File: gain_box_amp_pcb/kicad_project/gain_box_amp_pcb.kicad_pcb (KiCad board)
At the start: 2 copper layers, 80 x 100 mm, 58 parts, among them J1 Conn_01x02, J2 Conn_01x02, J3 Conn_01x02, J4 Conn_01x02, J5 Conn_01x02, J6 Conn_01x02, J7 Conn_01x02, J8 Conn_01x03, J9 Conn_01x04, K1 J104D2C12VDC.36S, K2 J104D2C12VDC.36S, K3 G5V-1, U1 NE5532, U2 NE5532, U3 NE5532, U4 140817141310

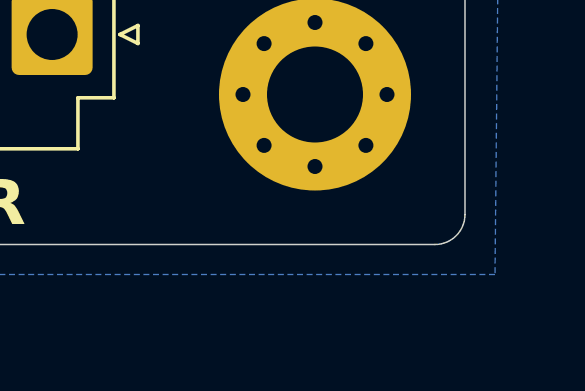
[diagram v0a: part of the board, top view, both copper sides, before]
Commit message: Shorten PSU PCB
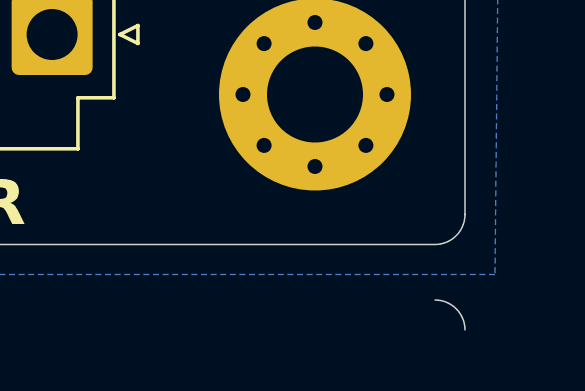
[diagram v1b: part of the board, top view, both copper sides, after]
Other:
- board size 80 x 100 mm -> 80 x 102.9 mm
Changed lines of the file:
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@@
 		(tags "SOD-123")
 		(property "Reference" "D2"
-			(at 3.5 -0.25 270)
+			(at 3.5 -0.25 -90)
 			(layer "F.SilkS")
 			(effects
@@
 		(tags "SOD-123")
 		(property "Reference" "D3"
-			(at 3.5 -0.25 270)
+			(at 3.5 -0.25 -90)
 			(layer "F.SilkS")
 			(effects
@@
 		(stroke
 			(width 0.05)
+			(type default)
+		)
+		(layer "Edge.Cuts")
+	)
+	(gr_arc
+		(start 225 137.85)
+		(mid 225.707107 138.142893)
+		(end 226 138.85)
+		(stroke
+			(width 0.05)

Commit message: Fix routing error
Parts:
- K3: value G5V-1 -> J104D2C12VDC.36S
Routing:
- net Net-(C8-Pad1): track 22.6 -> 23.3 mm
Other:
- board size 80 x 102.9 mm -> 80 x 100 mm

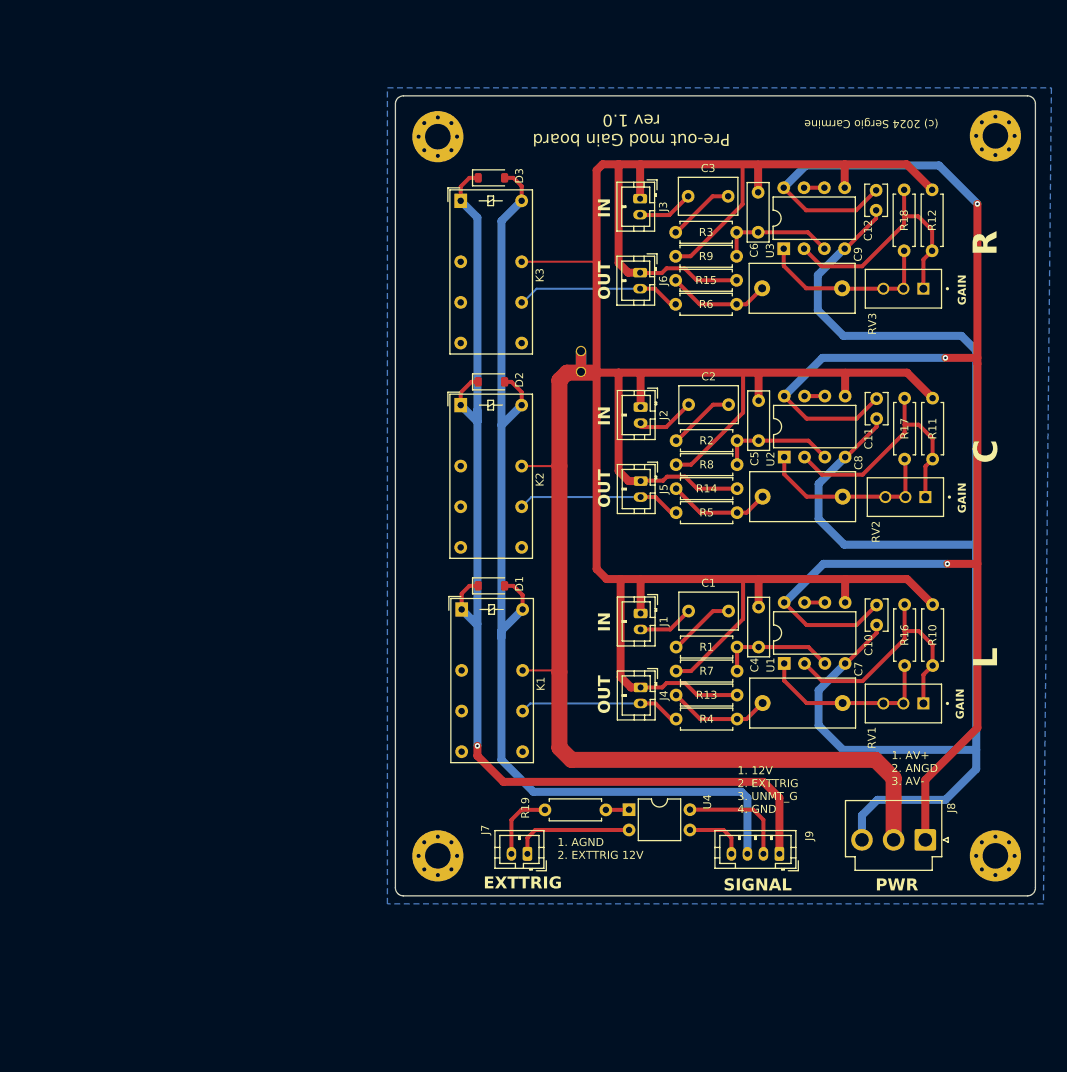
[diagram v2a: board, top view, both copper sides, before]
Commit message: Route new amp board
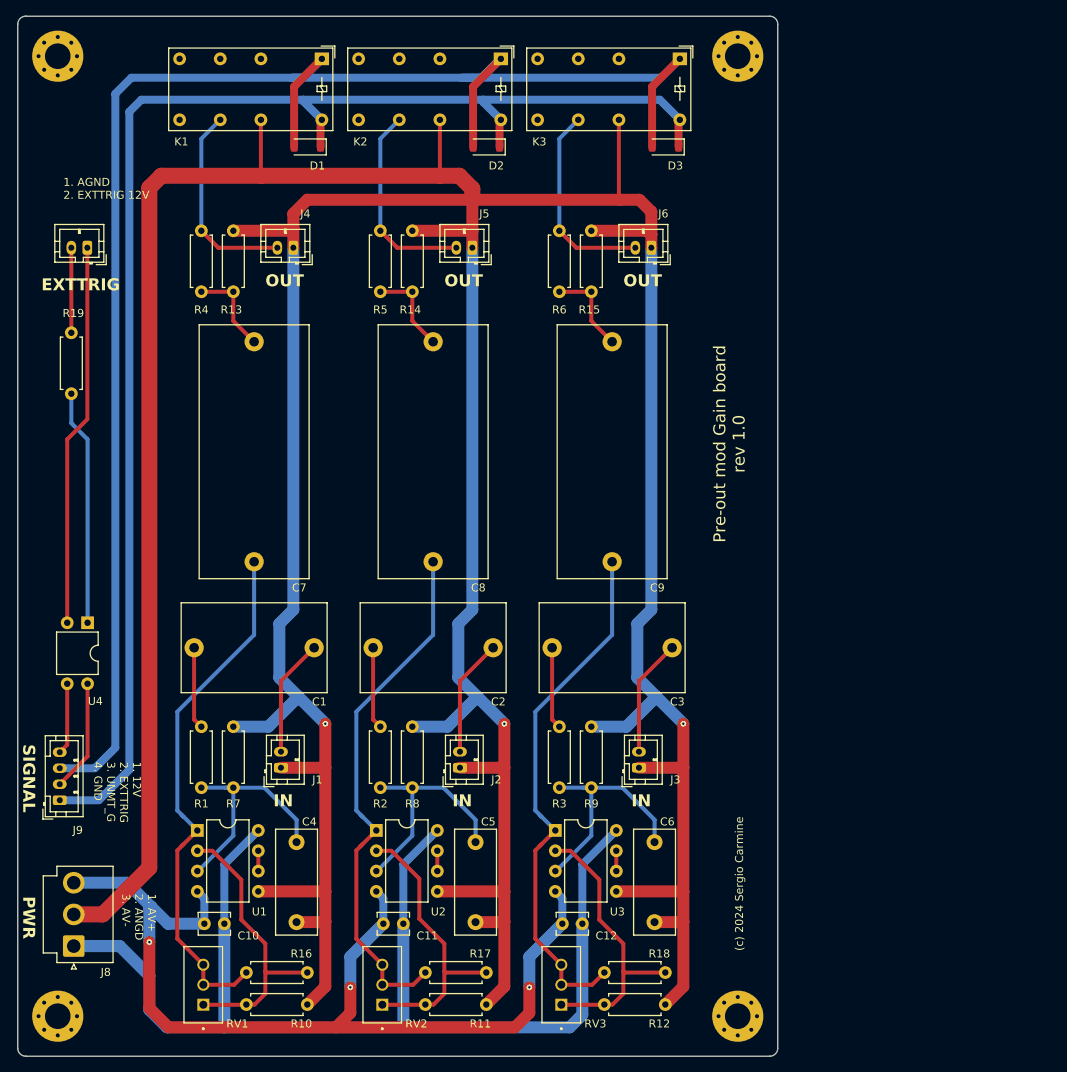
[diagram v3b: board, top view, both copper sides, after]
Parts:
- removed NT1: NetTie_2, NetTie:NetTie-2_THT_Pad1.0mm
- C1, C2, C3: footprint Capacitor_THT:C_Rect_L7.2mm_W4.5mm_P5.00mm_FKS2_FKP2_MKS2_MKP2 -> Capacitor_THT:C_Rect_L18.0mm_W11.0mm_P15.00mm_FKS3_FKP3
- C4, C5, C6: footprint Capacitor_THT:C_Rect_L7.2mm_W2.5mm_P5.00mm_FKS2_FKP2_MKS2_MKP2 -> Capacitor_THT:C_Rect_L13.0mm_W5.0mm_P10.00mm_FKS3_FKP3_MKS4
- C7, C8, C9: footprint Capacitor_THT:C_Rect_L13.0mm_W6.0mm_P10.00mm_FKS3_FKP3_MKS4 -> project_lib:C_Rect_L31.5mm_W12.5mm_P27.50mm_MKS4
- moved H4 118.9 mm to (103.8, 151.0), turned to -90 degrees
- moved H1 114.7 mm to (188.8, 151.0), turned to -90 degrees
- moved H3 110.7 mm to (103.8, 31.0), turned to -90 degrees
- moved J8 107.3 mm to (105.8, 142.3), turned to 90 degrees
- moved R12 102.7 mm to (172.1, 149.6), turned to 0 degrees
- moved R18 102.3 mm to (179.7, 145.6), turned to 180 degrees
- moved C12 97.4 mm to (166.9, 139.5), turned to 0 degrees
- moved RV3 96.9 mm to (166.7, 147.1), turned to 90 degrees
- moved R10 95.7 mm to (127.4, 149.6), turned to 0 degrees
- moved RV1 94.3 mm to (122.0, 147.1), turned to 90 degrees
- moved J7 93.6 mm to (107.5, 55.0)
- moved R11 93.1 mm to (149.7, 149.6), turned to 0 degrees
- moved C6 92.1 mm to (178.4, 139.3), turned to 90 degrees
- moved C10 92.0 mm to (122.1, 139.5), turned to 0 degrees
- moved J9 90.2 mm to (104.0, 124.0), turned to 90 degrees
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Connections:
- K1 pad A1: +12V -> UNMUTE_G
- K1 pad A2: UNMUTE_G -> +12V
- K2 pad A1: +12V -> UNMUTE_G
- K2 pad A2: UNMUTE_G -> +12V
- K3 pad A1: +12V -> UNMUTE_G
- K3 pad A2: UNMUTE_G -> +12V
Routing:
- net AGND: track 467.3 -> 625.3 mm, vias 0 -> 3
- net UNMUTE_G: track 132.1 -> 210.2 mm
- net AV-: track 190.5 -> 121.9 mm, vias 0 -> 3
- net AV+: track 203.1 -> 148.8 mm, vias 3 -> 0
- net Net-(C7-Pad1): track 23.0 -> 67.2 mm
- net Net-(C9-Pad1): track 23.1 -> 67.2 mm
- net Net-(C8-Pad1): track 23.3 -> 67.2 mm
- net +12V: track 137.5 -> 180.3 mm, vias 1 -> 0
- net Net-(J7-Pin_1): track 15.1 -> 47.9 mm
- net Net-(R19-Pad2): track 2.90 -> 29.5 mm
- net Net-(U1A-+): track 14.8 -> 29.7 mm
- net Net-(U3A-+): track 14.8 -> 29.7 mm
- net Net-(U2A-+): track 14.8 -> 29.7 mm
- net IN_FL: track 6.95 -> 14.7 mm
- net IN_FR: track 6.99 -> 14.7 mm
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- removed copper zone on B.Cu, net SHIELD
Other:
- board size 80 x 100 mm -> 95 x 130 mm
- board text removed: "C"
- board text removed: "GAIN"
- board text removed: "L"
- board text removed: "R"

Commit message: Sent to production
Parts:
- moved D1 0.18 mm to (135.2, 42.4)
- moved D2 0.18 mm to (157.6, 42.4)
- moved D3 0.18 mm to (179.9, 42.4)
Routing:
- net UNMUTE_G: track 210.2 -> 209.4 mm
- net +12V: track 180.3 -> 179.7 mm
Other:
- board text added: "(c) 2025 Sergio Carmine"
- board text added: "C"
- board text added: "JLCJLCJLCJLC"
- board text added: "L"
- board text added: "R"
- board text removed: "(c) 2024 Sergio Carmine"
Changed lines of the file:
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@@
 	(footprint "Diode_SMD:D_SOD-123"
 		(layer "F.Cu")
-		(at 179.740394 42.385394 180)
+		(at 179.925 42.385394 180)
 		(descr "SOD-123")
 		(tags "SOD-123")
@@
 	(footprint "Diode_SMD:D_SOD-123"
 		(layer "F.Cu")
-		(at 134.990394 42.385394 180)
+		(at 135.175 42.385394 180)
 		(descr "SOD-123")
 		(tags "SOD-123")
@@
 	(footprint "Diode_SMD:D_SOD-123"
 		(layer "F.Cu")
-		(at 157.365394 42.385394 180)
+		(at 157.55 42.385394 180)
 		(descr "SOD-123")
 		(tags "SOD-123")
@@
 		(layer "User.1")
 	)
+	(gr_text "JLCJLCJLCJLC"
+		(at 188.5 43.25 90)
+		(layer "B.SilkS")
+		(effects
+			(font
+				(size 1 1)
+				(thickness 0.15)
+			)
+			(justify mirror)
+		)
+	)
 	(gr_text "OUT"
 		(at 174.490394 59.985394 0)
@@
 		)
 	)
-	(gr_text "(c) 2024 Sergio Carmine "
+	(gr_text "(c) 2025 Sergio Carmine "
 		(at 188.990394 134.485394 90)
 		(layer "F.SilkS")
@@
 		)
 	)
+	(gr_text "C"
+		(at 148.5 49.25 0)
+		(layer "F.SilkS")
+		(effects
+			(font
+				(size 2.5 2.5)
+				(thickness 0.5)
+				(bold yes)
+			)
+			(justify left bottom)
+		)
+	)
 	(gr_text "IN"
 		(at 130.740394 124.985394 0)
@@
 		)
 	)
+	(gr_text "L"
+		(at 126.5 49.25 0)
+		(layer "F.SilkS")
+		(effects
+			(font
+				(size 2.5 2.5)
+				(thickness 0.5)
+				(bold yes)
+			)
+			(justify left bottom)
+		)
+	)
 	(gr_text "1. 12V\n2. EXTTRIG\n3. UNMT_G\n4. GND"
 		(at 108.240394 119.235394 -90)
@@
 		)
 	)
+	(gr_text "R"
+		(at 171.25 49.25 0)
+		(layer "F.SilkS")
+		(effects
+			(font
+				(size 2.5 2.5)
+				(thickness 0.5)
+				(bold yes)
+			)
+			(justify left bottom)
+		)
+	)
 	(gr_text "1. AGND\n2. EXTTRIG 12V"
 		(at 104.490394 48.985394 0)
@@
 	)
 	(segment
-		(start 136.640394 39.160394)
+		(start 136.807894 42.217894)
 		(end 136.807894 38.992894)
-		(width 1)
-		(layer "F.Cu")
-		(net 9)
-	)
-	(segment
-		(start 159.015394 39.160394)
-		(end 159.182894 38.992894)
-		(width 1)
+		(width 0.75)
 		(layer "F.Cu")
 		(net 9)
 	)
 	(segment
-		(start 181.390394 39.160394)
+		(start 181.557894 42.368288)
 		(end 181.557894 38.992894)
-		(width 1)
-		(layer "F.Cu")
-		(net 9)
-	)
-	(segment
-		(start 159.015394 42.385394)
-		(end 159.015394 39.160394)
-		(width 1)
+		(width 0.75)
 		(layer "F.Cu")
 		(net 9)
 	)
 	(segment
-		(start 136.640394 42.385394)
-		(end 136.640394 39.160394)
-		(width 1)
+		(start 159.2 42.200788)
+		(end 159.2 39.01)
+		(width 0.75)
 		(layer "F.Cu")
 		(net 9)
 	)
 	(segment
-		(start 181.390394 42.385394)
-		(end 181.390394 39.160394)
+		(start 159.2 39.01)
+		(end 159.182894 38.992894)
 		(width 1)
 		(layer "F.Cu")
@@
 		(start 159.182894 38.992894)
 		(end 156.990394 36.800394)
-		(width 1)
+		(width 0.75)
 		(layer "B.Cu")
 		(net 9)
@@
 		(start 179.050394 36.485394)
 		(end 181.557894 38.992894)
-		(width 1)
+		(width 0.75)
 		(layer "B.Cu")
 		(net 9)
@@
 		(start 136.807894 38.992894)
 		(end 134.490394 36.675394)
-		(width 1)
+		(width 0.75)
 		(layer "B.Cu")
 		(net 9)
@@
 		(start 114.240394 36.485394)
 		(end 134.490394 36.485394)
-		(width 1)
+		(width 0.75)
 		(layer "B.Cu")
 		(net 9)
@@
 		(start 112.740394 120.235394)
 		(end 112.740394 37.985394)
-		(width 1)
+		(width 0.75)
 		(layer "B.Cu")
 		(net 9)
@@
 		(start 112.740394 37.985394)
 		(end 114.240394 36.485394)
-		(width 1)
+		(width 0.75)
 		(layer "B.Cu")
 		(net 9)
@@
 		(start 134.490394 36.675394)
 		(end 134.490394 36.485394)
-		(width 1)
+		(width 0.75)
 		(layer "B.Cu")
 		(net 9)
@@
 		(start 104.042893 124.042893)
 		(end 108.932895 124.042893)
-		(width 1)
+		(width 0.75)
 		(layer "B.Cu")
 		(net 9)
@@
 		(start 156.990394 36.485394)
 		(end 179.050394 36.485394)
-		(width 1)
+		(width 0.75)
 		(layer "B.Cu")
 		(net 9)
@@
 		(start 134.490394 36.485394)
 		(end 156.990394 36.485394)
-		(width 1)
+		(width 0.75)
 		(layer "B.Cu")
 		(net 9)
@@
 		(start 108.932895 124.042893)
 		(end 112.740394 120.235394)
-		(width 1)
+		(width 0.75)
 		(layer "B.Cu")
 		(net 9)
@@
 		(start 156.990394 36.800394)
 		(end 156.990394 36.485394)
-		(width 1)
+		(width 0.75)
 		(layer "B.Cu")
 		(net 9)
 	)
 	(segment
-		(start 133.340394 34.840394)
-		(end 136.807894 31.372894)
-		(width 1)
+		(start 178.275 34.655788)
+		(end 181.557894 31.372894)
+		(width 0.75)
 		(layer "F.Cu")
 		(net 10)
 	)
 	(segment
-		(start 155.715394 34.840394)
-		(end 159.182894 31.372894)
-		(width 1)
+		(start 133.525 42.200788)
+		(end 133.525 34.655788)
+		(width 0.75)
 		(layer "F.Cu")
 		(net 10)
 	)
 	(segment
-		(start 133.340394 42.385394)
-		(end 133.340394 34.840394)
-		(width 1)
+		(start 133.525 34.655788)
+		(end 136.807894 31.372894)
+		(width 0.75)
 		(layer "F.Cu")
 		(net 10)
 	)
 	(segment
-		(start 178.090394 34.840394)
-		(end 181.557894 31.372894)
-		(width 1)
+		(start 155.9 42.200788)
+		(end 155.9 34.655788)
+		(width 0.75)
 		(layer "F.Cu")
 		(net 10)
 	)
 	(segment
-		(start 155.715394 42.385394)
-		(end 155.715394 34.840394)
-		(width 1)
+		(start 178.275 42.200788)
+		(end 178.275 34.655788)
+		(width 0.75)
 		(layer "F.Cu")
 		(net 10)
 	)
 	(segment
-		(start 178.090394 42.385394)
-		(end 178.090394 34.840394)
-		(width 1)
+		(start 155.9 34.655788)
+		(end 159.182894 31.372894)
+		(width 0.75)
 		(layer "F.Cu")
 		(net 10)
@@
 		(start 112.990394 33.735394)
 		(end 134.490394 33.735394)
-		(width 1)
+		(width 0.75)
 		(layer "B.Cu")
 		(net 10)
@@
 		(start 104.042893 120.042893)
 		(end 108.432895 120.042893)
-		(width 1)
+		(width 0.75)
 		(layer "B.Cu")
 		(net 10)
@@
 		(start 136.807894 31.417894)
 		(end 136.807894 31.372894)
-		(width 1)
+		(width 0.75)
 		(layer "B.Cu")
 		(net 10)
@@
 		(start 179.195394 33.735394)
 		(end 154.240394 33.735394)
-		(width 1)
+		(width 0.75)
 		(layer "B.Cu")
 		(net 10)
@@
 		(start 159.102894 31.372894)
 		(end 156.740394 33.735394)
-		(width 1)
+		(width 0.75)
 		(layer "B.Cu")
 		(net 10)
@@
 		(start 110.990394 35.735394)
 		(end 112.990394 33.735394)
-		(width 1)
+		(width 0.75)
 		(layer "B.Cu")
 		(net 10)
@@
 		(start 156.740394 33.735394)
 		(end 132.990394 33.735394)
-		(width 1)
+		(width 0.75)
 		(layer "B.Cu")
 		(net 10)
@@
 		(start 110.990394 117.485394)
 		(end 110.990394 35.735394)
-		(width 1)
+		(width 0.75)
 		(layer "B.Cu")
 		(net 10)
@@
 		(start 134.490394 33.735394)
 		(end 136.807894 31.417894)
-		(width 1)
+		(width 0.75)
 		(layer "B.Cu")
 		(net 10)
@@
 		(start 159.182894 31.372894)
 		(end 159.102894 31.372894)
-		(width 1)
+		(width 0.75)
 		(layer "B.Cu")
 		(net 10)
@@
 		(start 108.432895 120.042893)
 		(end 110.990394 117.485394)
-		(width 1)
+		(width 0.75)
 		(layer "B.Cu")
 		(net 10)
@@
 		(start 181.557894 31.372894)
 		(end 179.195394 33.735394)
-		(width 1)
+		(width 0.75)
 		(layer "B.Cu")
 		(net 10)
